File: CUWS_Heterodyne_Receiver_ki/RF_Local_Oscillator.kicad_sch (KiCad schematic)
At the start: 0 parts

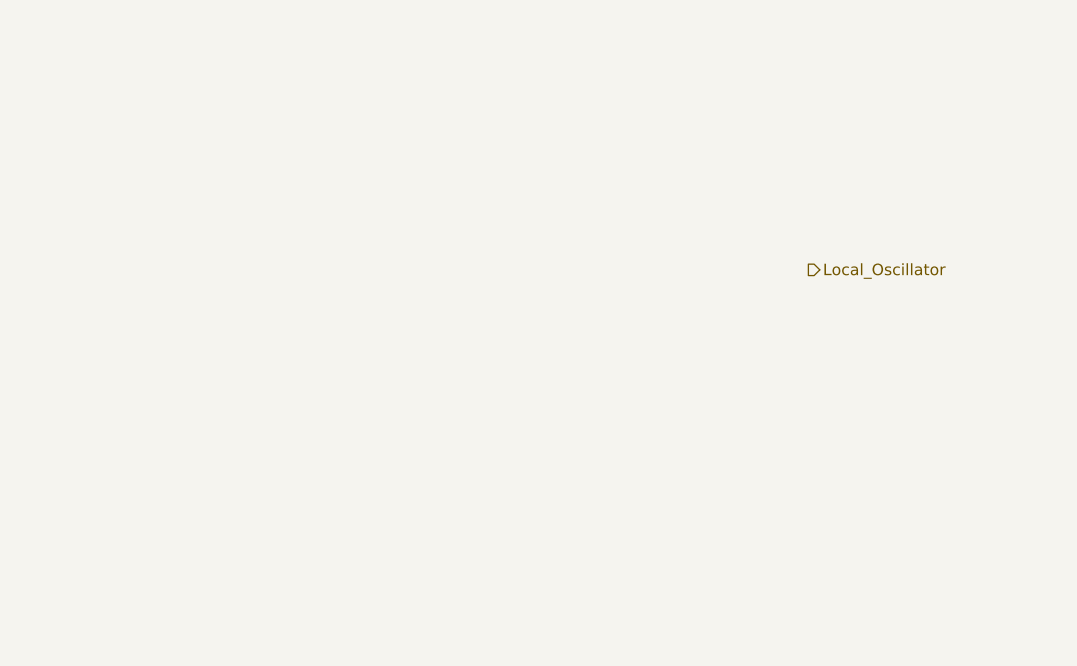
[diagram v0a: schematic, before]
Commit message: added oscilator LTspice file, the LTSpice sim works but the kicad one doesn't
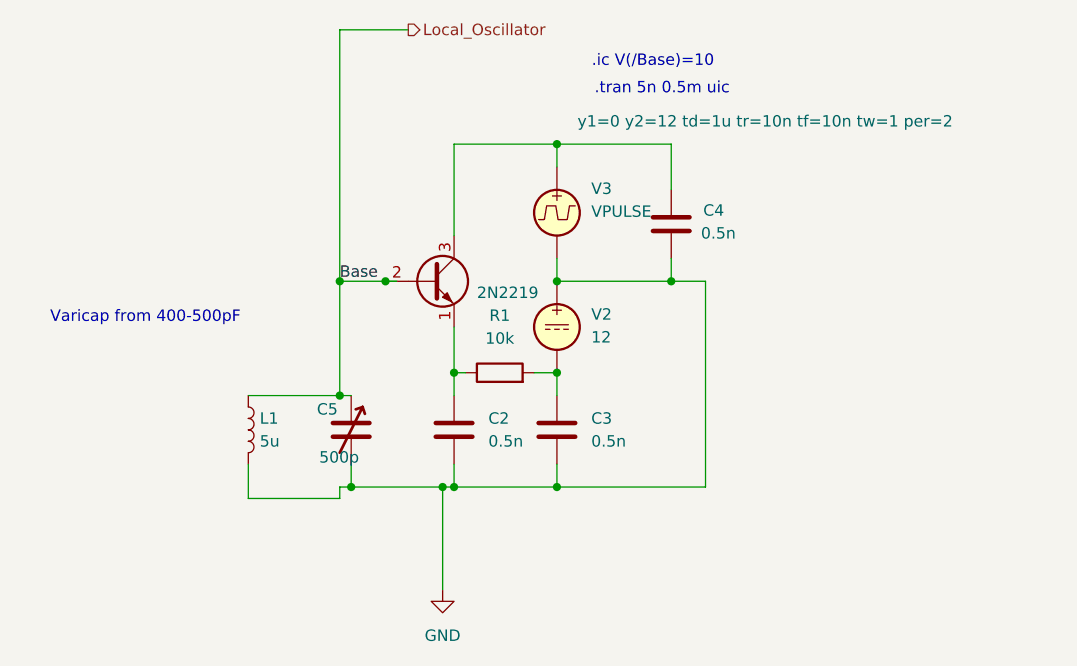
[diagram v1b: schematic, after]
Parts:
- added C2, C3, C4: 0.5n, symbol Device:C
- added C5: 500p, symbol Device:C_Variable
- added L1: 5u, symbol Device:L
- added Q1: 2N2219, Package_TO_SOT_THT:TO-39-3, symbol Transistor_BJT:2N2219
- added R1: 10k, symbol Device:R
- added V2: 12, symbol Simulation_SPICE:VDC
- added V3: VPULSE, symbol Simulation_SPICE:VPULSE
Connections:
- net Local_Oscillator: now also C5.1, L1.1, Q1.2 (B)
- new net: C3.1, R1.2, V2.2
- new net: C4.1, Q1.3 (C), V3.1
- new net: C2.1, Q1.1 (E), R1.1
- new net GND: C2.2, C3.2, C4.2, C5.2, L1.2, V2.1, V3.2
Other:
- note added: ".ic V(/Base)=10"
- note added: ".tran 5n 0.5m uic"
- note added: "Varicap from 400-500pF"
